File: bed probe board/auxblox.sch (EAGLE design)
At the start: 4 parts, among them CN1 3p-2.54, CN2 3p-2.54

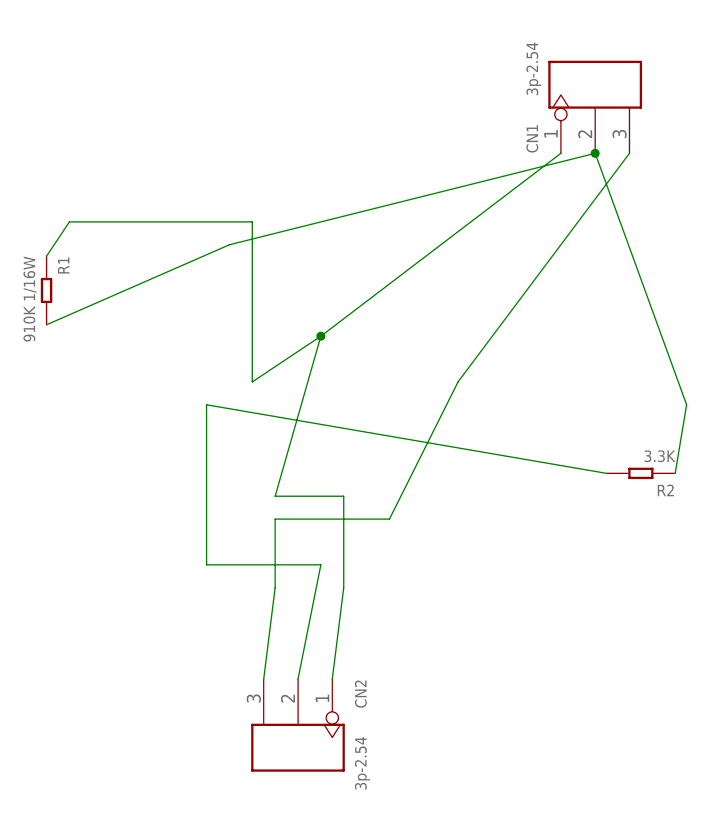
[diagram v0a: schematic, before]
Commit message: update bed probe board
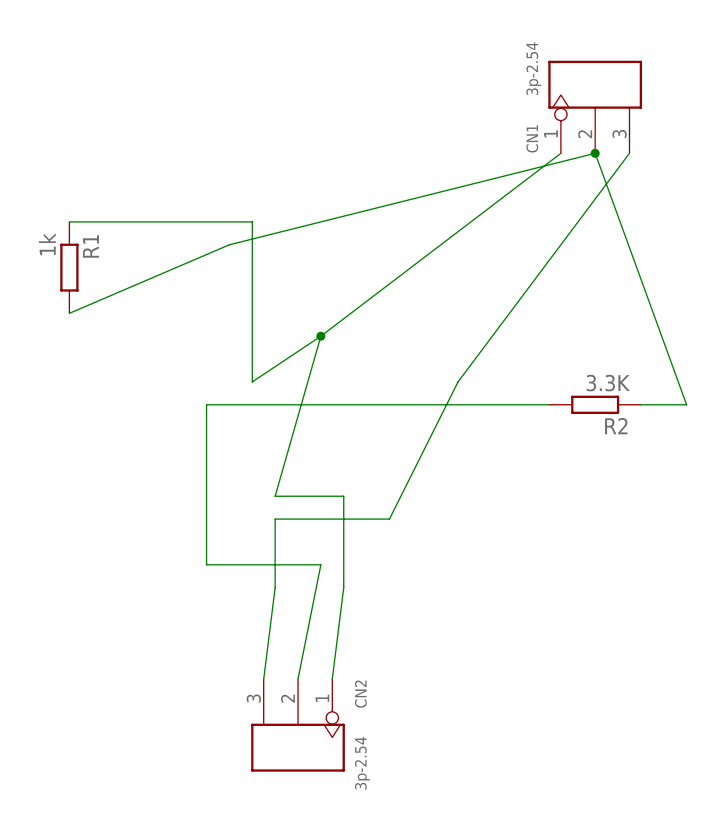
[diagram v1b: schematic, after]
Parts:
- R1: value 910K 1/16W -> 1k; device Seeed-Resistor-2016:SMD-RES-910K-5%-1/16W(0402) -> resistor:R-EU_R0805
- R2: device Seeed-Resistor-2016:SMD-RES-3.3K-5%-1/16W(0402) -> resistor:R-EU_R0805
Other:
- moved on the sheet: R1, R2
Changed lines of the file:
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@@
 <?xml version="1.0" encoding="utf-8"?>
 <!DOCTYPE eagle SYSTEM "eagle.dtd">
-<eagle version="7.5.0">
+<eagle version="7.6.0">
 <drawing>
 <settings>
@@
 <grid distance="0.1" unitdist="inch" unit="inch" style="lines" multiple="1" display="no" altdistance="0.01" altunitdist="inch" altunit="inch"/>
 <layers>
-<layer number="1" name="Top" color="4" fill="1" visible="no" active="no"/>
-<layer number="16" name="Bottom" color="1" fill="1" visible="no" active="no"/>
-<layer number="17" name="Pads" color="2" fill="1" visible="no" active="no"/>
-<layer number="18" name="Vias" color="2" fill="1" visible="no" active="no"/>
-<layer number="19" name="Unrouted" color="6" fill="1" visible="no" active="no"/>
-<layer number="20" name="Dimension" color="15" fill="1" visible="no" active="no"/>
-<layer number="21" name="tPlace" color="7" fill="1" visible="no" active="no"/>
-<layer number="22" name="bPlace" color="7" fill="1" visible="no" active="no"/>
-<layer number="23" name="tOrigins" color="15" fill="1" visible="no" active="no"/>
-<layer number="24" name="bOrigins" color="15" fill="1" visible="no" active="no"/>
-<layer number="25" name="tNames" color="7" fill="1" visible="no" active="no"/>
-<layer number="26" name="bNames" color="7" fill="1" visible="no" active="no"/>
-<layer number="27" name="tValues" color="7" fill="1" visible="no" active="no"/>
-<layer number="28" name="bValues" color="7" fill="1" visible="no" active="no"/>
+<layer number="1" name="Top" color="4" fill="1" visible="yes" active="no"/>
+<layer number="16" name="Bottom" color="1" fill="1" visible="yes" active="no"/>
+<layer number="17" name="Pads" color="2" fill="1" visible="yes" active="no"/>
+<layer number="18" name="Vias" color="2" fill="1" visible="yes" active="no"/>
+<layer number="19" name="Unrouted" color="6" fill="1" visible="yes" active="no"/>
+<layer number="20" name="Dimension" color="15" fill="1" visible="yes" active="no"/>
+<layer number="21" name="tPlace" color="7" fill="1" visible="yes" active="no"/>
+<layer number="22" name="bPlace" color="7" fill="1" visible="yes" active="no"/>
+<layer number="23" name="tOrigins" color="15" fill="1" visible="yes" active="no"/>
+<layer number="24" name="bOrigins" color="15" fill="1" visible="yes" active="no"/>
+<layer number="25" name="tNames" color="7" fill="1" visible="yes" active="no"/>
+<layer number="26" name="bNames" color="7" fill="1" visible="yes" active="no"/>
+<layer number="27" name="tValues" color="7" fill="1" visible="yes" active="no"/>
+<layer number="28" name="bValues" color="7" fill="1" visible="yes" active="no"/>
 <layer number="29" name="tStop" color="7" fill="3" visible="no" active="no"/>
 <layer number="30" name="bStop" color="7" fill="6" visible="no" active="no"/>
@@
 <layer number="35" name="tGlue" color="7" fill="4" visible="no" active="no"/>
 <layer number="36" name="bGlue" color="7" fill="5" visible="no" active="no"/>
-<layer number="37" name="tTest" color="7" fill="1" visible="no" active="no"/>
-<layer number="38" name="bTest" color="7" fill="1" visible="no" active="no"/>
+<layer number="37" name="tTest" color="7" fill="1" visible="yes" active="no"/>
+<layer number="38" name="bTest" color="7" fill="1" visible="yes" active="no"/>
 <layer number="39" name="tKeepout" color="4" fill="11" visible="no" active="no"/>
 <layer number="40" name="bKeepout" color="1" fill="11" visible="no" active="no"/>
@@
 <layer number="44" name="Drills" color="7" fill="1" visible="no" active="no"/>
 <layer number="45" name="Holes" color="7" fill="1" visible="no" active="no"/>
-<layer number="46" name="Milling" color="3" fill="1" visible="no" active="no"/>
-<layer number="47" name="Measures" color="7" fill="1" visible="no" active="no"/>
-<layer number="48" name="Document" color="7" fill="1" visible="no" active="no"/>
-<layer number="49" name="Reference" color="7" fill="1" visible="no" active="no"/>
-<layer number="50" name="dxf" color="7" fill="1" visible="no" active="no"/>
-<layer number="51" name="tDocu" color="7" fill="1" visible="no" active="no"/>
-<layer number="52" name="bDocu" color="7" fill="1" visible="no" active="no"/>
-<layer number="53" name="tGND_GNDA" color="7" fill="9" visible="no" active="no"/>
-<layer number="54" name="bGND_GNDA" color="1" fill="9" visible="no" active="no"/>
-<layer number="56" name="wert" color="7" fill="1" visible="no" active="no"/>
-<layer number="57" name="tCAD" color="7" fill="1" visible="no" active="no"/>
-<layer number="59" name="tCarbon" color="7" fill="1" visible="no" active="no"/>
-<layer number="60" name="bCarbon" color="7" fill="1" visible="no" active="no"/>
+<layer number="46" name="Milling" color="3" fill="1" visible="yes" active="no"/>
+<layer number="47" name="Measures" color="7" fill="1" visible="yes" active="no"/>
+<layer number="48" name="Document" color="7" fill="1" visible="yes" active="no"/>
+<layer number="49" name="Reference" color="7" fill="1" visible="yes" active="no"/>
+<layer number="50" name="dxf" color="7" fill="1" visible="yes" active="no"/>
+<layer number="51" name="tDocu" color="7" fill="1" visible="yes" active="no"/>
+<layer number="52" name="bDocu" color="7" fill="1" visible="yes" active="no"/>
+<layer number="53" name="tGND_GNDA" color="7" fill="9" visible="yes" active="no"/>
+<layer number="54" name="bGND_GNDA" color="1" fill="9" visible="yes" active="no"/>
+<layer number="56" name="wert" color="7" fill="1" visible="yes" active="no"/>
+<layer number="57" name="tCAD" color="7" fill="1" visible="yes" active="no"/>
+<layer number="59" name="tCarbon" color="7" fill="1" visible="yes" active="no"/>
+<layer number="60" name="bCarbon" color="7" fill="1" visible="yes" active="no"/>
 <layer number="90" name="Modules" color="5" fill="1" visible="no" active="yes"/>
 <layer number="91" name="Nets" color="2" fill="1" visible="yes" active="yes"/>
@@
 </classes>
 <parts>
-<part name="R1" library="Seeed-Resistor-2016" deviceset="SMD-RES-910K-5%-1/16W(0402)" device="" value="910K 1/16W"/>
-<part name="R2" library="Seeed-Resistor-2016" deviceset="SMD-RES-3.3K-5%-1/16W(0402)" device="" value="3.3K"/>
+<part name="R1" library="resistor" deviceset="R-EU_" device="R0805" value="1k"/>
+<part name="R2" library="resistor" deviceset="R-EU_" device="R0805" value="3.3K"/>
 <part name="FRAME1" library="frames" deviceset="FRAME_A_L" device=""/>
 <part name="FRAME2" library="frames" deviceset="FRAME_A_L" device=""/>
@@
 </plain>
 <instances>
-<instance part="R1" gate="G$1" x="81.28" y="195.58" rot="R270"/>
-<instance part="R2" gate="G$1" x="147.32" y="175.26" rot="R180"/>
+<instance part="R1" gate="G$1" x="83.82" y="198.12" rot="R270"/>
+<instance part="R2" gate="G$1" x="142.24" y="182.88" rot="R180"/>
 <instance part="FRAME1" gate="G$1" x="7.62" y="55.88"/>
 <instance part="FRAME1" gate="G$2" x="180.34" y="55.88"/>
@@
 <junction x="111.76" y="190.5"/>
 <pinref part="R1" gate="G$1" pin="1"/>
-<wire x1="81.28" y1="199.39" x2="83.82" y2="203.2" width="0.1524" layer="91"/>
 </segment>
 </net>
@@
 <wire x1="111.76" y1="165.1" x2="109.22" y2="152.4" width="0.1524" layer="91"/>
 <pinref part="R2" gate="G$1" pin="2"/>
-<wire x1="143.51" y1="175.26" x2="99.06" y2="182.88" width="0.1524" layer="91"/>
+<wire x1="137.16" y1="182.88" x2="99.06" y2="182.88" width="0.1524" layer="91"/>
 <wire x1="99.06" y1="182.88" x2="99.06" y2="165.1" width="0.1524" layer="91"/>
 <wire x1="99.06" y1="165.1" x2="111.76" y2="165.1" width="0.1524" layer="91"/>
@@
 <pinref part="CN1" gate="G$1" pin="P$2"/>
 <wire x1="142.24" y1="210.82" x2="152.4" y2="182.88" width="0.1524" layer="91"/>
-<wire x1="152.4" y1="182.88" x2="151.13" y2="175.26" width="0.1524" layer="91"/>
+<wire x1="152.4" y1="182.88" x2="147.32" y2="182.88" width="0.1524" layer="91"/>
 <pinref part="R2" gate="G$1" pin="1"/>
 <wire x1="142.24" y1="210.82" x2="101.6" y2="200.66" width="0.1524" layer="91"/>
-<wire x1="101.6" y1="200.66" x2="81.28" y2="191.77" width="0.1524" layer="91"/>
+<wire x1="101.6" y1="200.66" x2="83.82" y2="193.04" width="0.1524" layer="91"/>
 <junction x="142.24" y="210.82"/>
 <pinref part="R1" gate="G$1" pin="2"/>
@@
 </sheet>
 </sheets>
+<errors>
+</errors>
 </schematic>
 </drawing>
